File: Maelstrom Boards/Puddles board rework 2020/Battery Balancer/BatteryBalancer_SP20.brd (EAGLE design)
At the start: 101.6 x 101.6 mm, 84 parts, among them IC3 REG1117, P2 39-30-16?, Q1 SPB80P06P, Q2 SPB80P06P, Q3 NMOSFET-D2PAK-7, Q4 310mA/60V/1.6Ω, Q5 NMOSFET-D2PAK-7

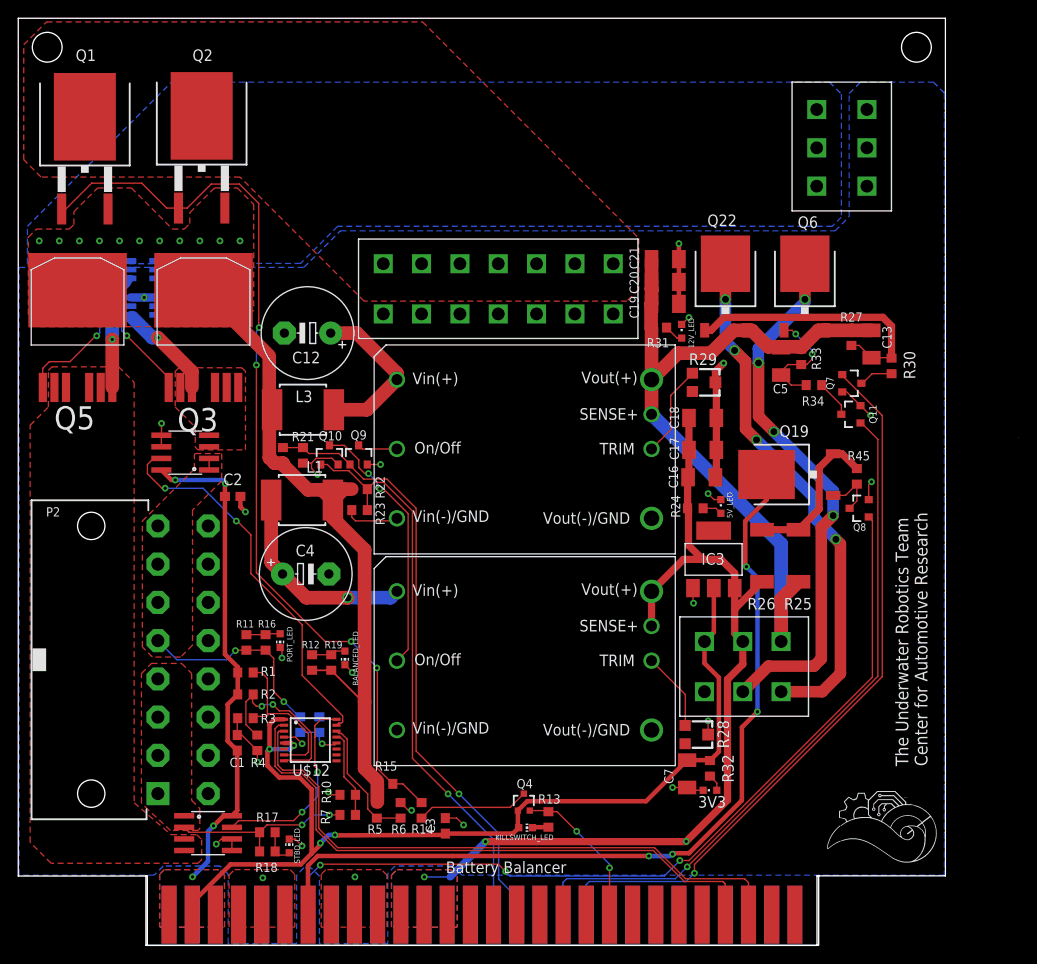
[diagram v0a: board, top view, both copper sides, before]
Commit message: final commit for ESC board, resistor values changed across boards for order ease
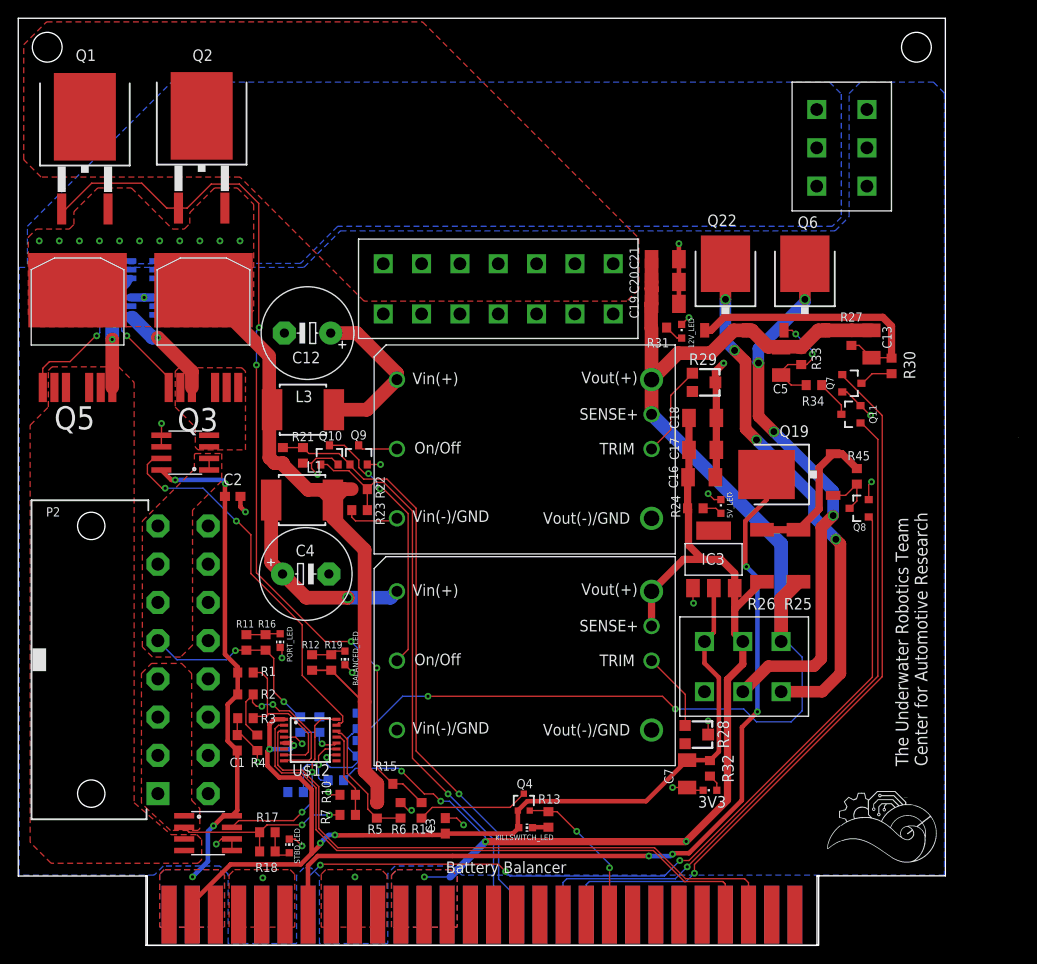
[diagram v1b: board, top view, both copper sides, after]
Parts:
- added R35, R37: 100k, rcl:R0603
- added R36: 20k, rcl:R0603
- added R38: 40k, rcl:R0603
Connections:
- new net N$31: R37.1, R38.2, U$12.IN6
- new net N$32: R35.2, R36.2, U$12.IN5
- net +12V: now also R37.2
- net +5V: now also R35.1
- net GND: now also R36.1, R38.1
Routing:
- net +12V: track 83.7 -> 145.0 mm, vias 0 -> 2
- net +5V: track 100.0 -> 118.0 mm, vias 3 -> 5
- net N$31: track 0.00 -> 10.5 mm, vias 0 -> 1
- net N$32: track 0.00 -> 10.3 mm, vias 0 -> 1
- net BALANCED_OUT: track 79.6 -> 78.3 mm

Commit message: Changing puddles values
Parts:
- 3V3: value (none) -> Green
- R24: value 90 -> 100
- R38: value 40k -> 39k
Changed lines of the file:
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@@
 <?xml version="1.0" encoding="utf-8"?>
 <!DOCTYPE eagle SYSTEM "eagle.dtd">
-<eagle version="9.5.2">
+<eagle version="9.6.2">
 <drawing>
 <settings>
@@
 <attribute name="VALUE" x="34.8242" y="70.3258" size="1.27" layer="27" ratio="10" rot="R180"/>
 </element>
-<element name="R24" library="rcl" library_urn="urn:adsk.eagle:library:334" package="R0603" package3d_urn="urn:adsk.eagle:package:23555/2" value="90" x="74.2" y="47.9" smashed="yes" rot="R180">
+<element name="R24" library="rcl" library_urn="urn:adsk.eagle:library:334" package="R0603" package3d_urn="urn:adsk.eagle:package:23555/2" value="100" x="74.2" y="47.9" smashed="yes" rot="R180">
 <attribute name="NAME" x="71.535" y="49.335" size="1.016" layer="25" rot="R270"/>
 <attribute name="SPICEPREFIX" value="R" x="85.4" y="89.2" size="1.778" layer="27" rot="R180" display="off"/>
@@
 <attribute name="VALUE" x="77.705" y="18.765" size="1.27" layer="27" rot="R90"/>
 </element>
-<element name="3V3" library="led" library_urn="urn:adsk.eagle:library:259" package="CHIPLED_0603" package3d_urn="urn:adsk.eagle:package:15822/2" value="" x="75.8" y="17" smashed="yes" rot="R90">
+<element name="3V3" library="led" library_urn="urn:adsk.eagle:library:259" package="CHIPLED_0603" package3d_urn="urn:adsk.eagle:package:15822/2" value="Green" x="75.8" y="17" smashed="yes" rot="R90">
 <attribute name="NAME" x="77.57" y="16.365" size="1.27" layer="25" rot="R180"/>
 <attribute name="VALUE" x="77.07" y="18.905" size="1.27" layer="27" rot="R180"/>
@@
 <attribute name="VALUE" x="35.295" y="20.965" size="1.27" layer="28" rot="MR90"/>
 </element>
-<element name="R38" library="rcl" library_urn="urn:adsk.eagle:library:334" package="R0603" package3d_urn="urn:adsk.eagle:package:23555/2" value="40k" x="37.2" y="24.6" smashed="yes" rot="MR270">
+<element name="R38" library="rcl" library_urn="urn:adsk.eagle:library:334" package="R0603" package3d_urn="urn:adsk.eagle:package:23555/2" value="39k" x="37.2" y="24.6" smashed="yes" rot="MR270">
 <attribute name="NAME" x="36.265" y="25.835" size="1.016" layer="26" rot="MR270"/>
 <attribute name="SPICEPREFIX" value="R" x="37.2" y="24.6" size="1.778" layer="28" rot="MR270" display="off"/>

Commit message: updates to puddles board rework actuator and BB.
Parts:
- added C14: 1000 uF, rcl:E5-13
- moved U$13 4.61 mm to (85.2, 87.2), turned to 270 degrees
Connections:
- net +12V: now also U$13.1+
- net BALANCED_OUT: now also C14.+; no longer U$13.1+
- net GND: now also C14.-
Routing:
- net +12V: track 145.0 -> 167.1 mm
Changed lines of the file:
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@@
 <?xml version="1.0" encoding="utf-8"?>
 <!DOCTYPE eagle SYSTEM "eagle.dtd">
-<eagle version="9.6.2">
+<eagle version="9.5.2">
 <drawing>
 <settings>
@@
 </element>
 <element name="Q22" library="transistor-fet" library_urn="urn:adsk.eagle:library:396" package="TO252" package3d_urn="urn:adsk.eagle:package:28537/2" value="" x="77.5" y="72.2" smashed="yes">
-<attribute name="NAME" x="78.74" y="80.09" size="1.27" layer="25" rot="R180"/>
+<attribute name="NAME" x="80.74" y="79.79" size="1.27" layer="25" rot="R180"/>
 <attribute name="VALUE" x="82.58" y="69.66" size="1.27" layer="27" rot="R90"/>
 </element>
@@
 <element name="U$5" library="Vertical_Connectors" package="6PIN_VERT" value="6PIN-VERT" x="75.2" y="33.3" smashed="yes" rot="R270"/>
 <element name="U$4" library="Vertical_Connectors" package="14PIN_VERT" value="14PIN-VERT" x="40" y="74.7" smashed="yes" rot="R270"/>
-<element name="U$13" library="Vertical_Connectors" package="6PIN_VERT" value="6PIN-VERT" x="87.5" y="83.2" smashed="yes"/>
+<element name="U$13" library="Vertical_Connectors" package="6PIN_VERT" value="6PIN-VERT" x="85.2" y="87.2" smashed="yes" rot="R270"/>
 <element name="R35" library="rcl" library_urn="urn:adsk.eagle:library:334" package="R0603" package3d_urn="urn:adsk.eagle:package:23555/2" value="100k" x="34.8" y="18.1" smashed="yes" rot="MR0">
 <attribute name="NAME" x="39.135" y="17.535" size="1.016" layer="26" rot="MR0"/>
@@
 <attribute name="VALUE" x="39.105" y="25.235" size="1.27" layer="28" rot="MR270"/>
 </element>
+<element name="C14" library="rcl" library_urn="urn:adsk.eagle:library:334" package="E5-13" package3d_urn="urn:adsk.eagle:package:23375/1" value="1000 uF" x="71.294971875" y="85.087865625" smashed="yes" rot="R315">
+<attribute name="NAME" x="63.842490625" y="88.828603125" size="1.778" layer="25" ratio="10" rot="R45"/>
+<attribute name="SPICEPREFIX" value="C" x="71.294971875" y="85.087865625" size="1.778" layer="27" rot="R315" display="off"/>
+<attribute name="VALUE" x="65.278203125" y="85.536878125" size="1.778" layer="27" ratio="10" rot="R315"/>
+</element>
 </elements>
 <signals>
@@
 <vertex x="31.3" y="74.3"/>
 <vertex x="35.3" y="78.3"/>
-<vertex x="89.5" y="78.3"/>
-<vertex x="91.048978125" y="79.848978125"/>
-<vertex x="91.048978125" y="93.348978125"/>
-<vertex x="92.3046125" y="94.6046125"/>
-<vertex x="100.285259375" y="94.6046125"/>
-<vertex x="101.5" y="93.389871875"/>
+<vertex x="65.3" y="78.3"/>
+<vertex x="71.989871875" y="84.989871875"/>
+<vertex x="101.5" y="84.989871875"/>
 <vertex x="101.5" y="7.7"/>
 <vertex x="48.6" y="7.7"/>
@@
 <wire x1="90.3" y1="60.65" x2="90.8" y2="60.65" width="0.1524" layer="1"/>
 <wire x1="90.8" y1="60.65" x2="92.3" y2="59.15" width="0.1524" layer="1"/>
+<contactref element="C14" pad="-"/>
 </signal>
 <signal name="+5V">
@@
 <wire x1="36.95" y1="19.4" x2="41.7" y2="19.4" width="0.1524" layer="16"/>
 <wire x1="47.25815" y1="15.8" x2="51.2" y2="11.85815" width="0.1524" layer="16"/>
-<wire x1="44.4655" y1="3.375" x2="44.5" y2="7.5" width="0" layer="19" extent="16-16"/>
 </signal>
 <signal name="+3V3">
@@
 <wire x1="27.817" y1="58.7" x2="27.5" y2="59.017" width="1.5" layer="1"/>
 <wire x1="27.5" y1="59.017" x2="27.5" y2="64.1" width="1.5" layer="1"/>
-<contactref element="U$13" pad="1+"/>
 <contactref element="U$13" pad="3+"/>
 <contactref element="U$13" pad="2+"/>
-<polygon width="0.1524" layer="16" thermals="no">
-<vertex x="30.934846875" y="74.734846875"/>
-<vertex x="15.9" y="74.734846875"/>
-<vertex x="15.9" y="74.7"/>
-<vertex x="1" y="74.7"/>
-<vertex x="1" y="78.8"/>
-<vertex x="16.8" y="94.6"/>
-<vertex x="88.9" y="94.6"/>
-<vertex x="90.2" y="93.3"/>
-<vertex x="90.2" y="79.8"/>
-<vertex x="89.2" y="78.8"/>
-<vertex x="35" y="78.8"/>
-</polygon>
 <via x="2.3" y="77.2" extent="1-16" drill="0.35"/>
 <via x="4.5" y="77.2" extent="1-16" drill="0.35"/>
@@
 <wire x1="39.35" y1="17.7" x2="39.35" y2="15.7" width="1.5" layer="1"/>
 <wire x1="39.35" y1="15.7" x2="39.3" y2="15.65" width="1.5" layer="1"/>
+<contactref element="C14" pad="+"/>
+<polygon width="0.1524" layer="16" thermals="no">
+<vertex x="29.3" y="74.8"/>
+<vertex x="31.2" y="74.8"/>
+<vertex x="35.1" y="78.7"/>
+<vertex x="64.8" y="78.7"/>
+<vertex x="71.7" y="85.6"/>
+<vertex x="101.2" y="85.6"/>
+<vertex x="101.4" y="85.8"/>
+<vertex x="101.4" y="101.5"/>
+<vertex x="3.4" y="101.5"/>
+<vertex x="0.6" y="98.7"/>
+<vertex x="0.6" y="75.1"/>
+</polygon>
 </signal>
 <signal name="N$11">
@@
 <wire x1="80.9" y1="24.5" x2="84.7" y2="24.5" width="0.1524" layer="16"/>
 <wire x1="85.9" y1="31.6" x2="84.2" y2="33.3" width="0.1524" layer="16"/>
+<contactref element="U$13" pad="1+"/>
+<wire x1="69.4" y1="75.2" x2="69.4" y2="77.5" width="1.5" layer="1"/>
+<wire x1="85" y1="87.2" x2="85.2" y2="87.2" width="1.5" layer="1"/>
+<wire x1="69.4" y1="77.5" x2="71.8" y2="79.9" width="1.5" layer="1"/>
+<wire x1="71.8" y1="79.9" x2="77.7" y2="79.9" width="1.5" layer="1"/>
+<wire x1="77.7" y1="79.9" x2="85" y2="87.2" width="1.5" layer="1"/>
 </signal>
 <signal name="N$18">
